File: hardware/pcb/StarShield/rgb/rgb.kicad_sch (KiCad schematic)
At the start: 95 parts

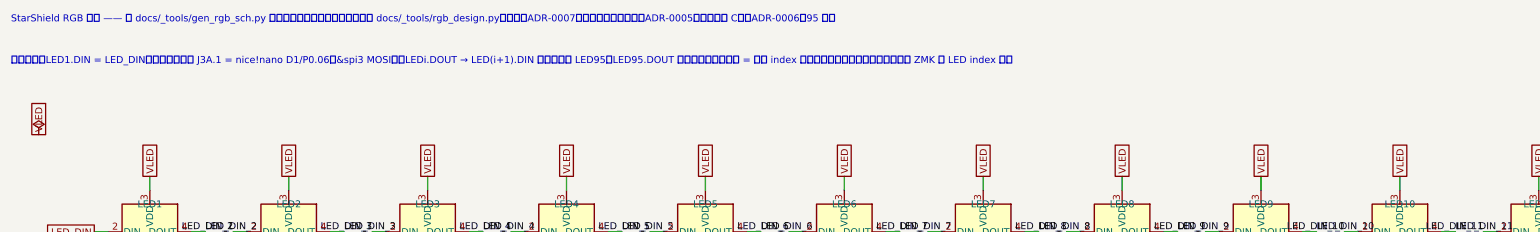
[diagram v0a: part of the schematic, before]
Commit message: fix(b6-1): J3A/J3B 由 1x12 改 1x13（按 nice!nano v2 实物孔序），走线零改动
背景：2026-09-19 实物核对发现 nice!nano v2 每排 13 孔（官方 pinout 图 + 实物清点），
原 1x12 设计会把 J3B 的 VCC 插到实物 RESET 上、J3A 整排错位一孔。

关键洞察：官方孔序去掉第 1 孔后与旧 12 孔的网**逐孔一致** ⇒
只需在 USB 端左侧（x=37.46）加一个孔（J3A 加 GND、J3B 加 OUT）+ Pad 号整体后移一位，
**走线一根都不用动**。（反面做法「网络整体后移一孔」实测撞出 8 处 shorting_items +
2 处 tracks_crossing，已否决。）

改动：
- extract_power_symbols.py：符号缓存加 Connector_Generic:Conn_01x13（取代 01x12）
- control_design.py：J3A/J3B 改 Conn_01x13、CONN 表按官方孔序重排、页脚注更新
- control.kicad_sch / rgb.kicad_sch：生成链重跑产物
- verify_control.py / verify_rgb.py：断言孔号同步（LED_DIN 由 J3A.1 改 J3A.2）
- rgb_design.py：注释里的 J3A.1 改 J3A 孔2
- Starshield.kicad_pcb：J3A/J3B 各加第 13 孔、Pad 号重排、J3B 孔1-孔2 OUT 同网桥、
  重填铺铜（未连通 0、未豁免 error 0）
- docs/nice-nano-physical-verification.md：§4 落点修正（座口 x≈32.2）、§6 量测结论与执行记录

校验：七项校验器全绿；生成链确定性复核通过（重跑生成器后 git status 无变化）。
固件 overlay 零改动（D 编号 ↔ GPIO 映射不变）。
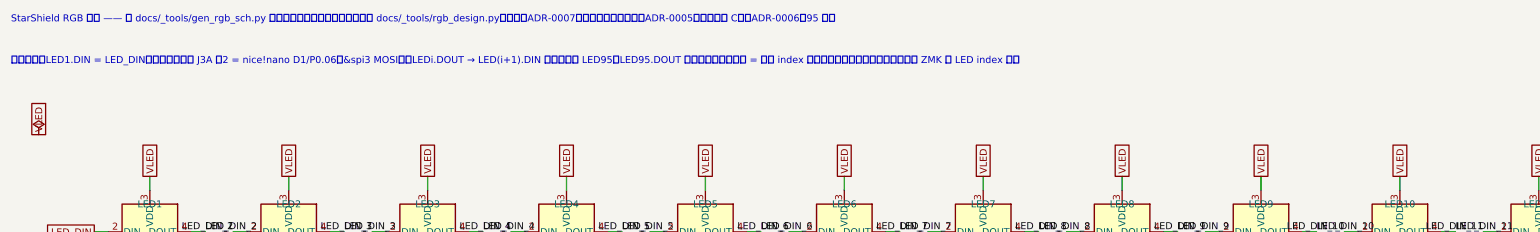
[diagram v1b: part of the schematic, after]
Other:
- note added: "【数据链】LED1.DIN = LED_DIN（来自控制子图 J3A 孔2 = nice!nano D1/P0.06，&spi3 MOSI）；LEDi.DOUT → LED(i+1).DIN 依次串联到 LED95；LED95.DOUT 悬空（链尾）。链序 = 键位 index 顺序（行优先、行内从左到右），与 ZMK 侧 LED index 一致"
- note removed: "【数据链】LED1.DIN = LED_DIN（来自控制子图 J3A.1 = nice!nano D1/P0.06，&spi3 MOSI）；LEDi.DOUT → LED(i+1).DIN 依次串联到 LED95；LED95.DOUT 悬空（链尾）。链序 = 键位 index 顺序（行优先、行内从左到右），与 ZMK 侧 LED index 一致"
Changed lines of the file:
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@@
 		(effects (font (size 1.27 1.27)) (justify left bottom))
 )
-	(text "【数据链】LED1.DIN = LED_DIN（来自控制子图 J3A.1 = nice!nano D1/P0.06，&spi3 MOSI）；LEDi.DOUT → LED(i+1).DIN 依次串联到 LED95；LED95.DOUT 悬空（链尾）。链序 = 键位 index 顺序（行优先、行内从左到右），与 ZMK 侧 LED index 一致" (exclude_from_sim no) (at 25.4 33.02 0)
+	(text "【数据链】LED1.DIN = LED_DIN（来自控制子图 J3A 孔2 = nice!nano D1/P0.06，&spi3 MOSI）；LEDi.DOUT → LED(i+1).DIN 依次串联到 LED95；LED95.DOUT 悬空（链尾）。链序 = 键位 index 顺序（行优先、行内从左到右），与 ZMK 侧 LED index 一致" (exclude_from_sim no) (at 25.4 33.02 0)
 		(effects (font (size 1.27 1.27)) (justify left bottom))
 )
